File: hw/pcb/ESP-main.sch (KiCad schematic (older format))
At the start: 5 parts, among them U201 MIC803, U202 ESP32-WROVER

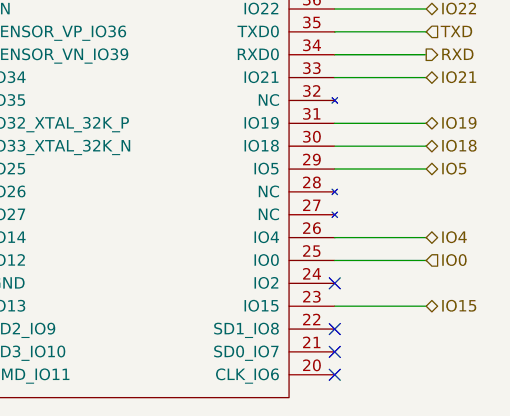
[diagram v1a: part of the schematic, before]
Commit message: fixed severe PCB issue, clearance of ground fills was too small, could lead to thermal instability
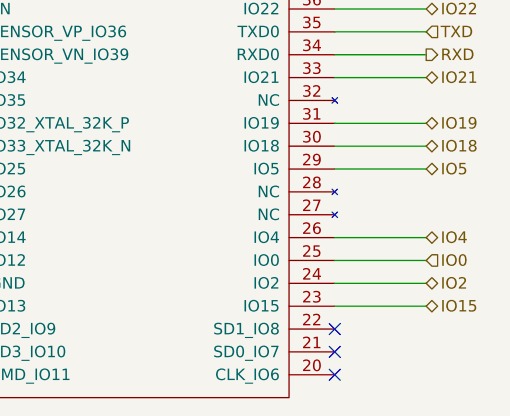
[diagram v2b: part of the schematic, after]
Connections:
- net IO2: now reaches U202.24 (IO2)
- no-connect marks 7 -> 6
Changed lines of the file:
@@
 encoding utf-8
 Sheet 2 6
-Title "CTAG-TBD"
-Date "2020-06-06"
-Rev "C"
+Title "ESP32 Eurorack Audio Module"
+Date "2020-08-18"
+Rev "G"
 Comp "(c) Robert Manzke 2020"
 Comment1 "https://creativecommons.org/licenses/by-nc-sa/4.0/"
@@
 	1    0    0    -1
 $EndComp
-NoConn ~ 6900 3350
+Text HLabel 7300 3350 2    50   BiDi ~ 0
+IO2
+Wire Wire Line
+	7300 3350 6900 3350
 $EndSCHEMATC

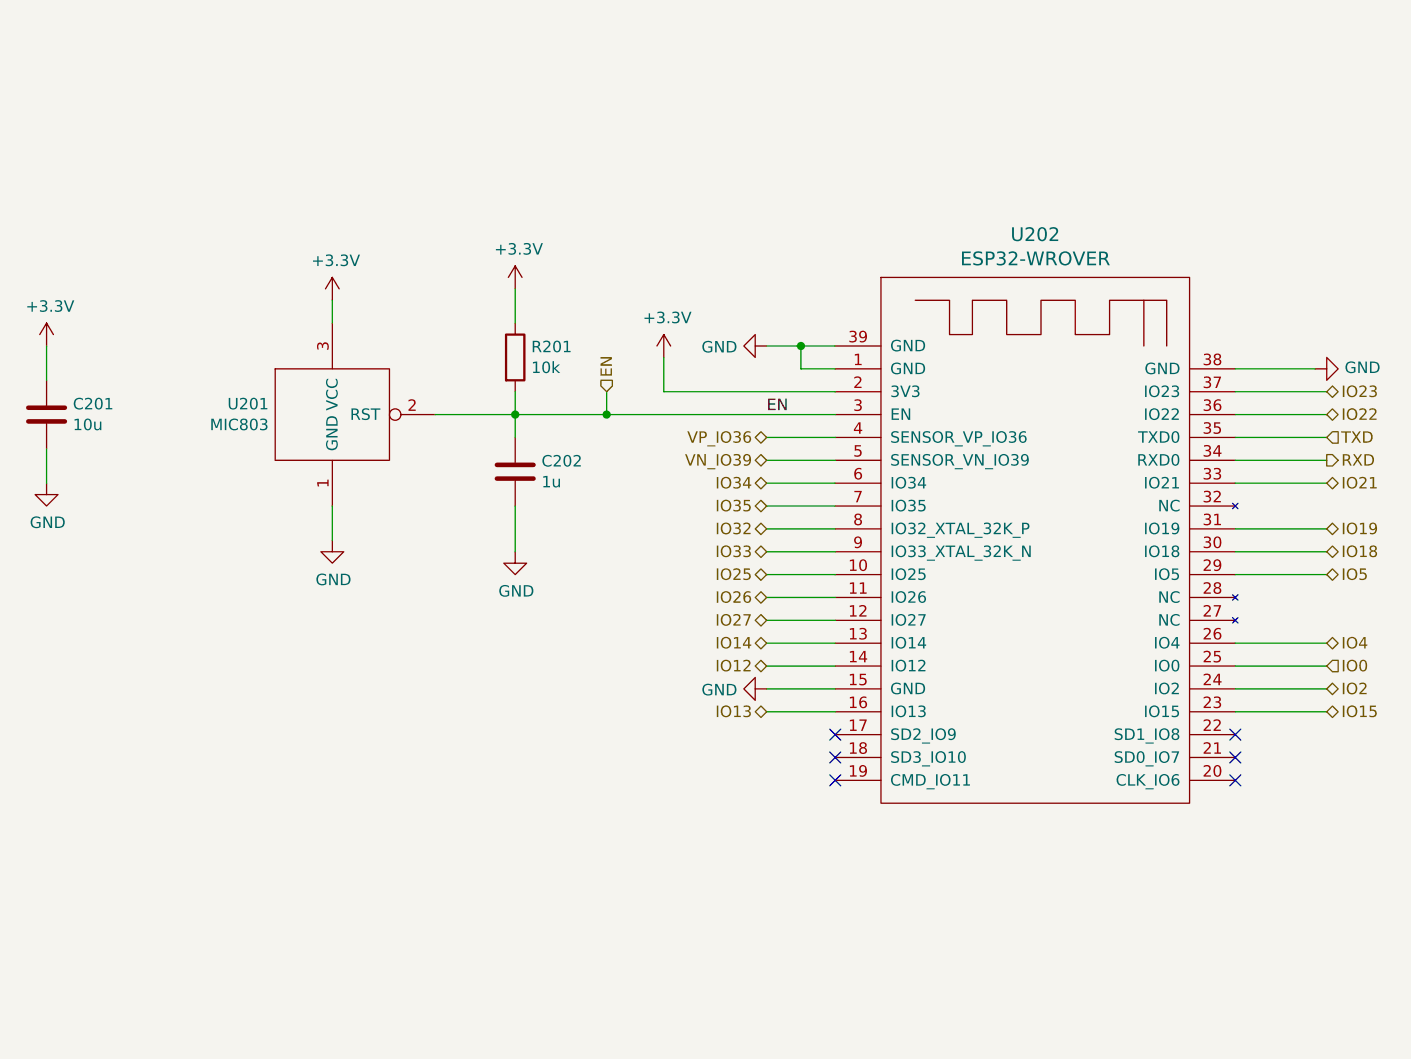
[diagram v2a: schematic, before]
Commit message: Updated Eurorack hw to Rev. H
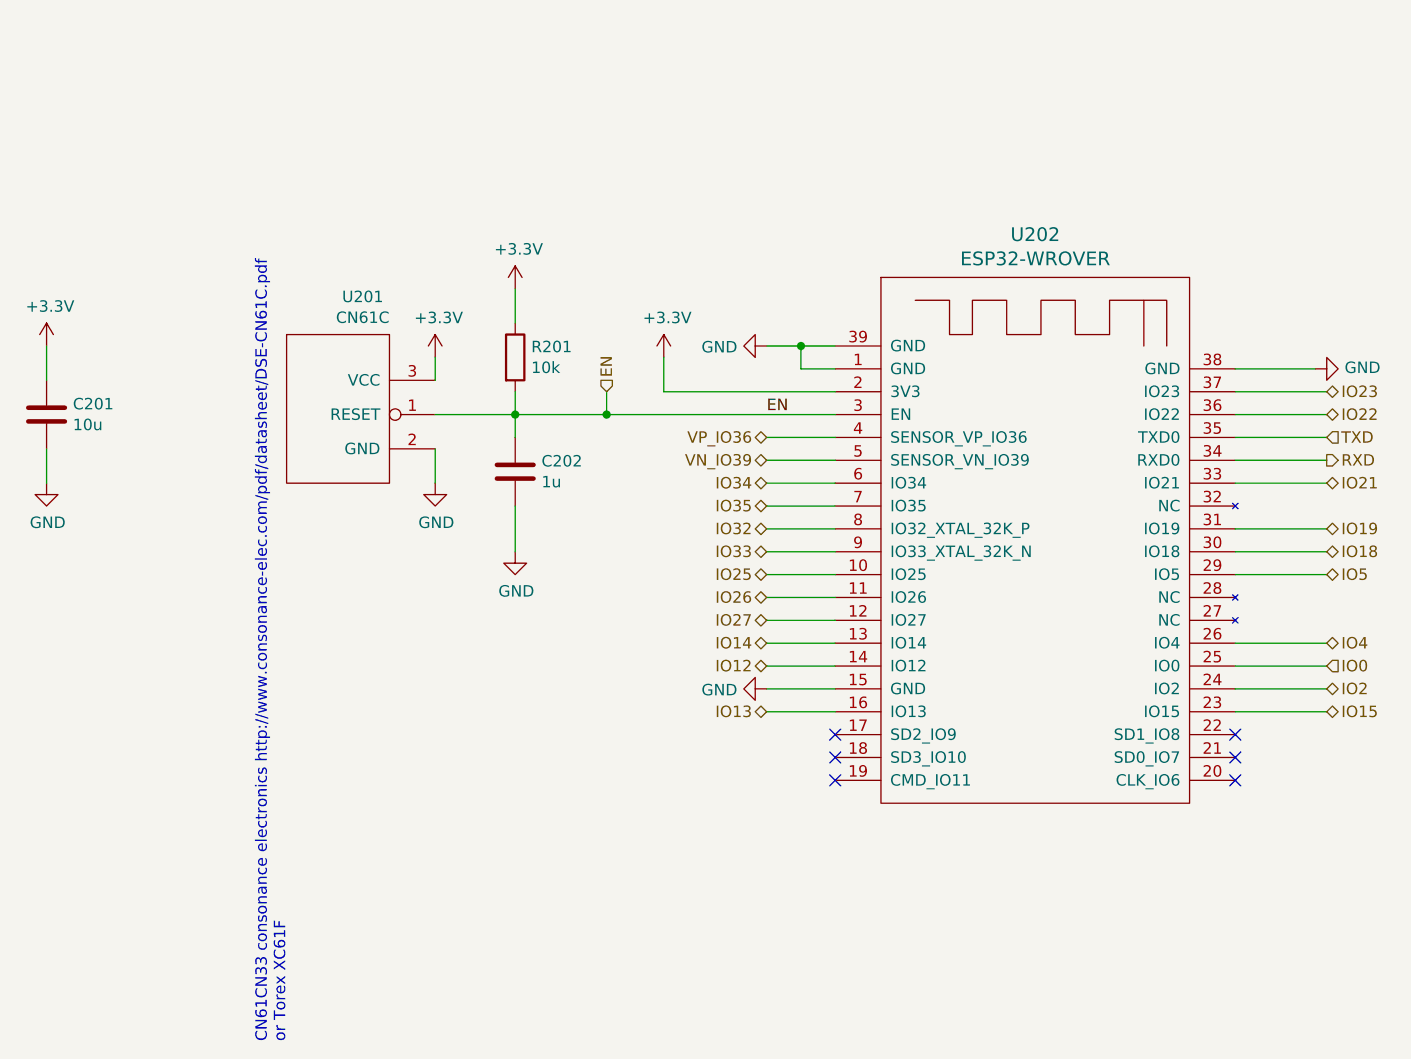
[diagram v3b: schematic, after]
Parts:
- removed U201: MIC803, Package_TO_SOT_SMD:SOT-23, symbol special-ics:MIC803
- added U201: CN61C, Package_TO_SOT_SMD:SOT-23, symbol special-ics:CN61C
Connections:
- net +3V3: now also U201.3 (VCC)
- net EN: now also U201.1 (RESET)
- net GND: now also U201.2 (GND)
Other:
- note added: "CN61CN33 consonance electronics http://www.consonance-elec.com/pdf/datasheet/DSE-CN61C.pdf\nor Torex XC61F"
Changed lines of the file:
@@
 Sheet 2 6
 Title "ESP32 Eurorack Audio Module"
-Date "2020-08-18"
-Rev "G"
-Comp "(c) Robert Manzke 2020"
+Date "2021-10-05"
+Rev "H"
+Comp "(c) Robert Manzke 2021"
 Comment1 "https://creativecommons.org/licenses/by-nc-sa/4.0/"
 Comment2 "Licensed under CC BY-NC-SA 4.0"
@@
 NoConn ~ 5150 3750
 $Comp
-L special-ics:MIC803 U201
-U 1 1 5CA3F4DA
-P 2950 2350
-F 0 "U201" H 2672 2596 50  0000 R CNN
-F 1 "MIC803" H 2672 2505 50  0000 R CNN
-F 2 "Package_TO_SOT_SMD:SOT-23" H 2950 2350 50  0001 C CNN
-F 3 "" H 2950 2350 50  0001 C CNN
-	1    2950 2350
-	1    0    0    -1
-$EndComp
-$Comp
 L power:+3.3V #PWR0202
 U 1 1 5CA450EC
-P 2950 1650
-F 0 "#PWR0202" H 2950 1500 50  0001 C CNN
-F 1 "+3.3V" H 2965 1823 50  0000 C CNN
-F 2 "" H 2950 1650 50  0001 C CNN
-F 3 "" H 2950 1650 50  0001 C CNN
-	1    2950 1650
-	1    0    0    -1
-$EndComp
-Wire Wire Line
-	2950 1650 2950 1750
+P 3400 1900
+F 0 "#PWR0202" H 3400 1750 50  0001 C CNN
+F 1 "+3.3V" H 3415 2073 50  0000 C CNN
+F 2 "" H 3400 1900 50  0001 C CNN
+F 3 "" H 3400 1900 50  0001 C CNN
+	1    3400 1900
+	1    0    0    -1
+$EndComp
+Wire Wire Line
+	3400 1900 3400 2000
 $Comp
 L power:GND #PWR0208
 U 1 1 5CA47446
-P 2950 2700
-F 0 "#PWR0208" H 2950 2450 50  0001 C CNN
-F 1 "GND" H 2955 2527 50  0000 C CNN
-F 2 "" H 2950 2700 50  0001 C CNN
-F 3 "" H 2950 2700 50  0001 C CNN
-	1    2950 2700
-	1    0    0    -1
-$EndComp
-Wire Wire Line
-	2950 2550 2950 2700
+P 3400 2450
+F 0 "#PWR0208" H 3400 2200 50  0001 C CNN
+F 1 "GND" H 3405 2277 50  0000 C CNN
+F 2 "" H 3400 2450 50  0001 C CNN
+F 3 "" H 3400 2450 50  0001 C CNN
+	1    3400 2450
+	1    0    0    -1
+$EndComp
+Wire Wire Line
+	3400 2300 3400 2450
 Wire Wire Line
 	3750 2150 3400 2150
@@
 Wire Wire Line
 	7300 3350 6900 3350
+$Comp
+L special-ics:CN61C U201
+U 1 1 61618AFA
+P 2750 1800
+F 0 "U201" H 3083 1965 50  0000 C CNN
+F 1 "CN61C" H 3083 1874 50  0000 C CNN
+F 2 "Package_TO_SOT_SMD:SOT-23" H 3000 1800 50  0001 C CNN
+F 3 "" H 3000 1800 50  0001 C CNN
+	1    2750 1800
+	1    0    0    -1
+$EndComp
+Text Notes 2750 4900 1    50   ~ 0
+CN61CN33 consonance electronics http://www.consonance-elec.com/pdf/datasheet/DSE-CN61C.pdf\nor Torex XC61F
 $EndSCHEMATC
